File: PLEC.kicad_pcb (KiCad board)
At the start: 4 copper layers, 84 parts, among them IC1 XBP9B-DMST-002, J1 Conn_01x02, J2 Conn_01x02, J3 Conn_01x03, J4 Conn_01x06, J5 Conn_01x04, K1 PB1167, K2 PB1167, K3 PB1167, K4 PB1167, Q1 KSC2073H2TU, U1 LM1085-5.0, U2 LM1085-3.3, U3 TLP222A-2, U4 TLP222A, U5 TLP222A-2, U6 HXS20, U7 NBPMANN150, U8 Teensy3.6

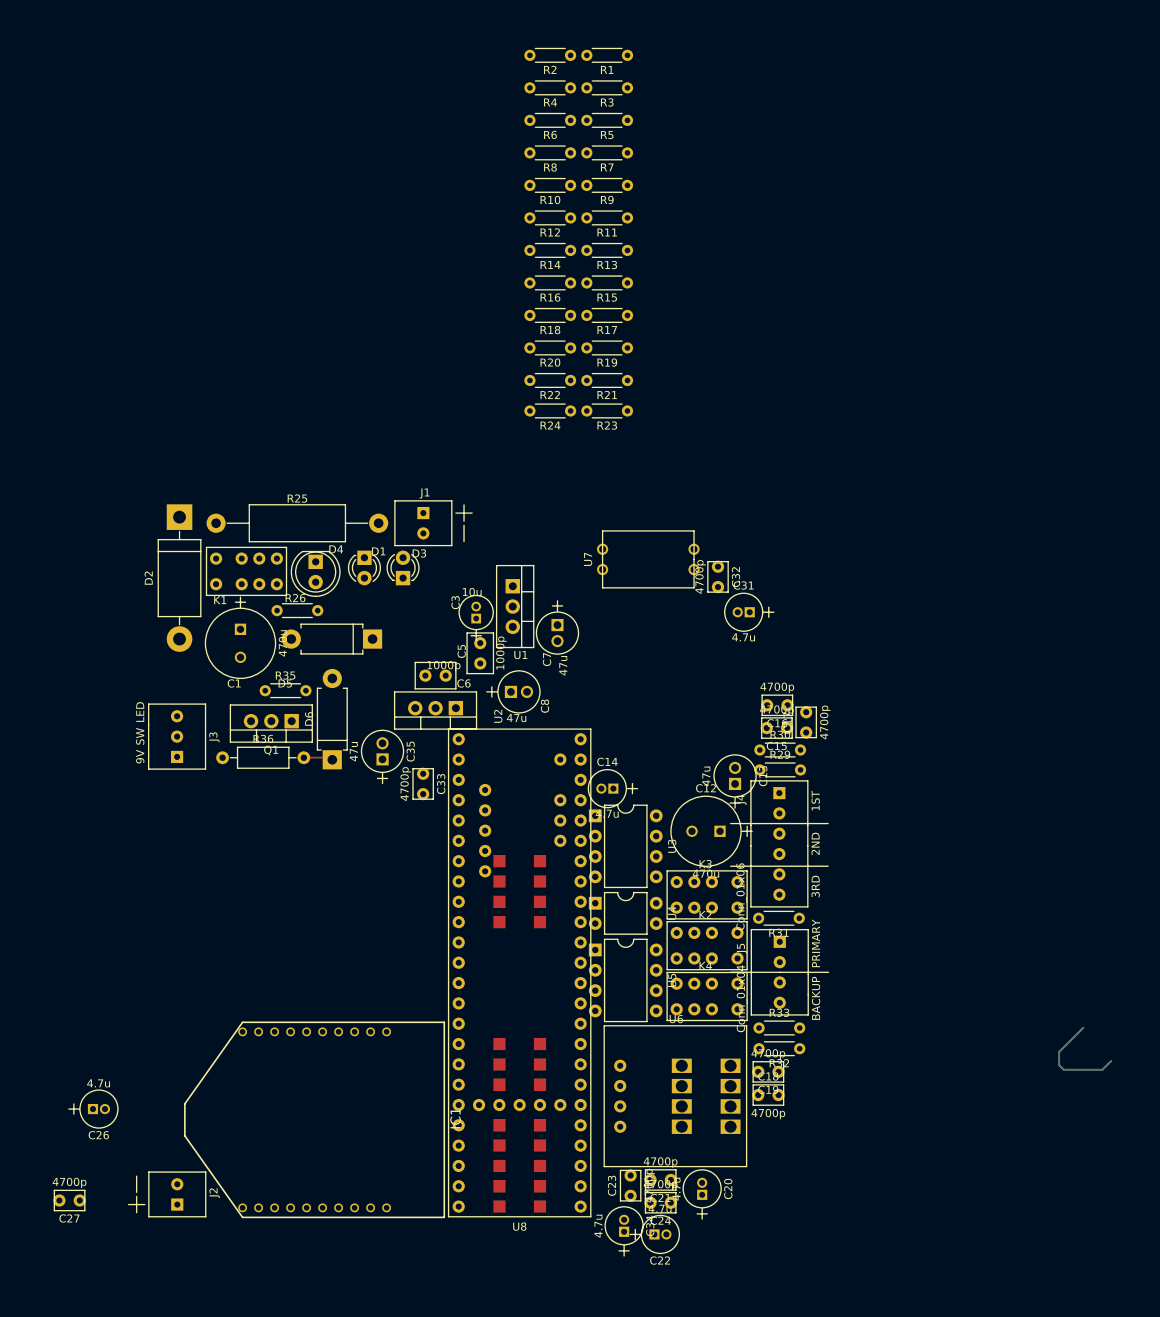
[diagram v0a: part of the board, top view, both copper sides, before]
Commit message: Almost done with layout; need to rearrange uC pins
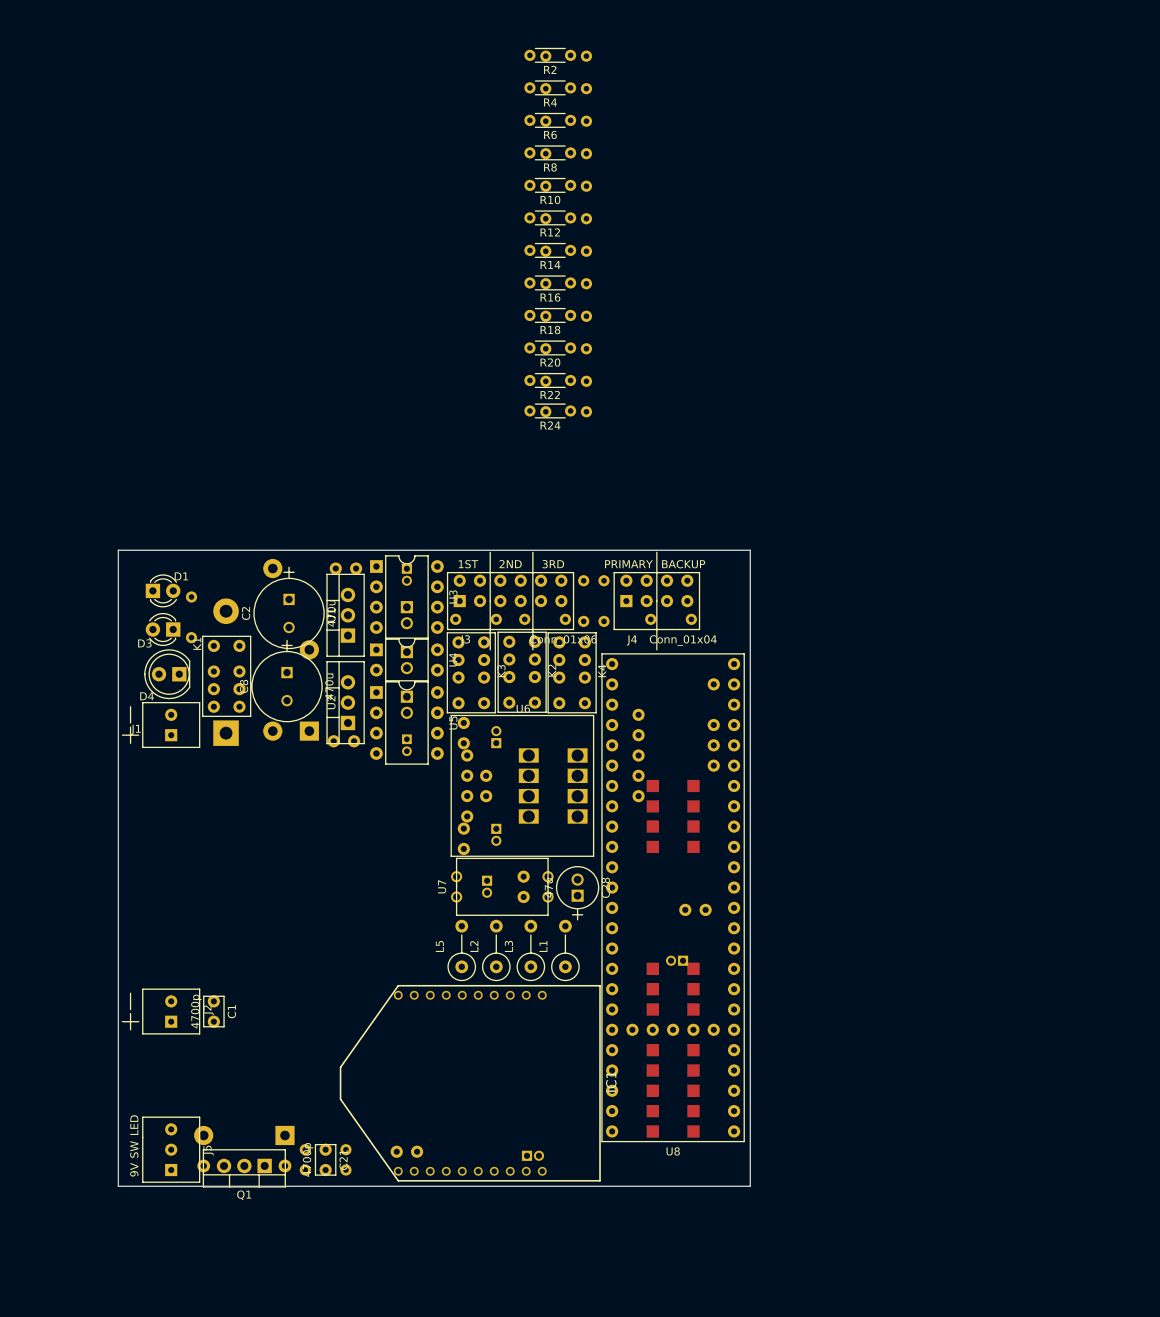
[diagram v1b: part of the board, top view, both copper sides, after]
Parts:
- removed C31, C34: 4.7u, PLEC:THTm_1.5Px4Dx7H_4.7u
- removed C32, C33: 4700p, PLEC:THTt_100Px150Lx100Wx183H_4700p
- removed C35: 47u, PLEC:THTm_2Px4Dx12H_47u
- removed R35: 100K, Resistors_THT:R_Axial_DIN0204_L3.6mm_D1.6mm_P5.08mm_Horizontal
- removed R36: 400, Resistors_THT:R_Axial_DIN0207_L6.3mm_D2.5mm_P10.16mm_Horizontal
- added C10: 4.7u, PLEC:THTm_1.5Px4Dx7H_4.7u, B.Cu at (138.9, 88.1)
- added C11: 4700p, PLEC:THTt_100Px150Lx100Wx183H_4700p, B.Cu at (146.8, 88.9)
- added C2: 470u, PLEC:THTm_5Px8Dx22H__470u, F.Cu at (124.2, 93.0)
- added C25: 4700p, PLEC:THTt_100Px150Lx100Wx183H_4700p, B.Cu at (153.5, 127.2)
- added C28: 47u, PLEC:THTm_2Px4Dx12H_47u, F.Cu at (160.3, 127.3)
- added C4: 1000p, PLEC:THTt_100Px200Lx125Wx200H_1000p, B.Cu at (131.3, 87.4)
- added C9: 47u, PLEC:THTm_2Px4Dx12H_47u, B.Cu at (138.9, 98.8)
- added L1: Ferrite_Bead_Small, Inductors_THT:L_Axial_L7.0mm_D3.3mm_P5.08mm_Vertical_Fastron_MICC, F.Cu at (158.8, 137.2)
- added L2: Ferrite_Bead_Small, Inductors_THT:L_Axial_L7.0mm_D3.3mm_P5.08mm_Vertical_Fastron_MICC, F.Cu at (150.1, 137.2)
- added L3: Ferrite_Bead_Small, Inductors_THT:L_Axial_L7.0mm_D3.3mm_P5.08mm_Vertical_Fastron_MICC, F.Cu at (154.4, 137.2)
- added L5: Ferrite_Bead_Small, Inductors_THT:L_Axial_L7.0mm_D3.3mm_P5.08mm_Vertical_Fastron_MICC, F.Cu at (145.8, 137.2)
- added R27: 100K, Resistors_THT:R_Axial_DIN0204_L3.6mm_D1.6mm_P5.08mm_Horizontal, B.Cu at (145.0, 93.7)
- added R28: 100K, Resistors_THT:R_Axial_DIN0204_L3.6mm_D1.6mm_P5.08mm_Horizontal, B.Cu at (153.7, 93.7)
- added R34: 400, Resistors_THT:R_Axial_DIN0207_L6.3mm_D2.5mm_P10.16mm_Horizontal, B.Cu at (113.5, 162.1)
- C1: value 470u -> 4700p; footprint PLEC:THTm_5Px8Dx22H__470u -> PLEC:THTt_100Px150Lx100Wx183H_4700p
- C12: value 470u -> 4700p; footprint PLEC:THTm_5Px8Dx22H__470u -> PLEC:THTt_100Px150Lx100Wx183H_4700p; moved to B.Cu
- C13: value 47u -> 4700p; footprint PLEC:THTm_2Px4Dx12H_47u -> PLEC:THTt_100Px150Lx100Wx183H_4700p; moved to B.Cu
- C14, C20, C26: value 4.7u -> 4700p; footprint PLEC:THTm_1.5Px4Dx7H_4.7u -> PLEC:THTt_100Px150Lx100Wx183H_4700p; moved to B.Cu
- C15, C17, C19, C22, C23, C3, C5, C7, D2, D5, D6, R1, R11, R13, R15, R17, R19, R21, R23, R25, R26, R29, R3, R30, R31, R32, R33, R5, R7, R9: moved to B.Cu
- C16, C18, C24, C27: value 4700p -> 4.7u; footprint PLEC:THTt_100Px150Lx100Wx183H_4700p -> PLEC:THTm_1.5Px4Dx7H_4.7u; moved to B.Cu
- C6: value 1000p -> 47u; footprint PLEC:THTt_100Px200Lx125Wx200H_1000p -> PLEC:THTm_2Px4Dx12H_47u; moved to B.Cu
- C8: value 47u -> 470u; footprint PLEC:THTm_2Px4Dx12H_47u -> PLEC:THTm_5Px8Dx22H__470u
- J3: value Conn_01x03 -> Conn_01x06; footprint PLEC:THT_TerminalBlock_2.5mm_3pos -> PLEC:THT_TerminalBlock_2.5mm_6pos
- J4: value Conn_01x06 -> Conn_01x04; footprint PLEC:THT_TerminalBlock_2.5mm_6pos -> PLEC:THT_TerminalBlock_2.5mm_4pos
- J5: value Conn_01x04 -> Conn_01x03; footprint PLEC:THT_TerminalBlock_2.5mm_4pos -> PLEC:THT_TerminalBlock_2.5mm_3pos
- moved C27 81.6 mm to (172.7, 136.4), turned to 180 degrees
- moved J5 81.2 mm to (109.5, 162.6), turned to 90 degrees
- moved C26 78.6 mm to (175.0, 130.0)
- moved R33 59.4 mm to (126.2, 162.6)
- moved R32 58.1 mm to (131.3, 160.0)
- moved C20 57.1 mm to (148.8, 114.6)
- moved C19 56.9 mm to (146.1, 108.0), turned to 90 degrees
- moved C18 56.2 mm to (150.1, 108.5), turned to 90 degrees
- moved Q1 55.7 mm to (121.2, 162.1)
- moved D6 47.3 mm to (123.7, 158.2), turned to 180 degrees
- moved C1 46.2 mm to (114.8, 142.7), turned to 90 degrees
- moved C17 45.2 mm to (146.1, 121.2)
- moved C24 45.1 mm to (149.0, 127.1), turned to 270 degrees
- moved U7 44.8 mm to (151.1, 127.2)
- moved U6 43.2 mm to (160.3, 110.7)
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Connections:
- C1 pad 1: V_9 -> Net-(C1-Pad1)
- C12 pad 1: SWITCH_RETURN -> EM_R2+
- C12 pad 2: GND -> EM_R2-
- C13 pad 1: SWITCH_RETURN -> EM_R3+
- C13 pad 2: GND -> EM_R3-
- C14 pad 1: SWITCH_RETURN -> EM_E1+
- C14 pad 2: GND -> EM_E1-
- C15 pad 1: EM_R1+ -> EM_E2+
- C15 pad 2: EM_R1- -> EM_E2-
- C16 pad 1: EM_R2+ -> CURR_REF
- C16 pad 2: EM_R2- -> GND
- C17 pad 1: EM_R3+ -> CURR_REF
- C17 pad 2: EM_R3- -> GND
- C18 pad 1: EM_E1+ -> V_5
- C18 pad 2: EM_E1- -> GND
- C19 pad 1: EM_E2+ -> V_5
- C19 pad 2: EM_E2- -> GND
- C20 pad 1: CURR_REF -> CurrentData_5V
- C21 pad 1: CURR_REF -> Net-(C21-Pad1)
- C22 pad 1: V_5 -> V_33
- C23 pad 1: V_5 -> V_33
- C24 pad 1: CurrentData_5V -> V_5
- C26 pad 1: V_33 -> V_5
- C26 pad 2: GND -> /Microcontroller/VEE
- C27 pad 1: V_33 -> V_5
- C27 pad 2: GND -> /Microcontroller/VEE
- C6 pad 1: Net-(C3-Pad1) -> V_5
- C7 pad 1: V_5 -> V_33
- C8 pad 1: V_33 -> SWITCH_RETURN
- J2 pad 1: ROVER_RELAY -> Net-(C1-Pad1)
- J2 pad 2: GND -> Net-(J2-Pad2)
- J3 pad 1: V_9 -> EM_R1+
- J3 pad 2: SWITCH_RETURN -> EM_R1-
- J3 pad 3: /LED_CATHODE -> EM_R2+
- J4 pad 1: EM_R1+ -> EM_E1+
- J4 pad 2: EM_R1- -> EM_E1-
- J4 pad 3: EM_R2+ -> EM_E2+
- J4 pad 4: EM_R2- -> EM_E2-
- J5 pad 1: EM_E1+ -> Net-(J5-Pad1)
- J5 pad 2: EM_E1- -> Net-(J5-Pad2)
- J5 pad 3: EM_E2+ -> /LED_CATHODE
- Q1 pad 1: LED_CONTROL -> Net-(C21-Pad1)
- R29 pad 1: EM_R1+ -> EM_R3+
- R29 pad 2: EM_R1- -> EM_R3-
- R30 pad 1: EM_R2+ -> EM_E1+
- R30 pad 2: EM_R2- -> EM_E1-
- R31 pad 1: EM_R3+ -> EM_E2+
- R31 pad 2: EM_R3- -> EM_E2-
- R32 pad 1: EM_E1+ -> Net-(C21-Pad1)
- R32 pad 2: EM_E1- -> LED_CONTROL
- R33 pad 1: EM_E2+ -> SWITCH_RETURN
- R33 pad 2: EM_E2- -> Net-(C21-Pad1)
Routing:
- net (no net): track 13.2 -> 0.00 mm
- net Net-(D6-Pad1): track 3.66 -> 0.00 mm
- net Net-(D2-Pad2): track 1.27 -> 0.00 mm
- net Net-(C3-Pad1): track 1.08 -> 0.00 mm
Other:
- board outline added: 79 x 79.5 mm

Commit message: Finished PCB with no errors
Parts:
- added C29: 4700p, PLEC:THTt_100Px150Lx100Wx183H_4700p, F.Cu at (114.7, 160.1)
- added G***: LOGO, PLEC:USLI_logo_820, B.Cu at (148.8, 151.6)
- added G***: LOGO, PLEC:USLI_logo_negative, F.Cu at (122.9, 149.4)
- added REF**: 1pin, Connectors:1pin, F.Cu at (110.2, 110.0)
- added REF**: 1pin, Connectors:1pin, F.Cu at (143.5, 136.4)
- added REF**: 1pin, Connectors:1pin, F.Cu at (141.5, 115.3)
- added REF**: 1pin, Connectors:1pin, F.Cu at (108.5, 151.1)
- added REF**: 1pin, Connectors:1pin, F.Cu at (173.7, 165.9)
- added REF**: 1pin, Connectors:1pin, F.Cu at (179.1, 95.8)
- added REF**: 1pin, Connectors:1pin, F.Cu at (116.1, 89.2)
- R2, R4: moved to B.Cu
- moved R2 113.2 mm to (174.1, 135.5), turned to 90 degrees
- moved R3 105.3 mm to (168.5, 132.0), turned to 90 degrees
- moved R4 101.8 mm to (170.9, 128.4), turned to 90 degrees
- moved R1 101.6 mm to (174.1, 123.3), turned to 270 degrees
- moved R9 83.0 mm to (173.0, 120.9), turned to 180 degrees
- moved R10 82.1 mm to (169.7, 120.9), turned to 0 degrees
- moved R5 79.8 mm to (178.1, 108.2), turned to 90 degrees
- moved R6 76.6 mm to (178.1, 105.7), turned to 270 degrees
- moved R11 76.6 mm to (173.0, 118.4), turned to 180 degrees
- moved R12 75.5 mm to (169.7, 118.4), turned to 0 degrees
- moved R13 70.1 mm to (173.0, 115.8), turned to 180 degrees
- moved R14 69.0 mm to (169.7, 115.8), turned to 0 degrees
- moved R7 66.1 mm to (174.4, 99.1)
- moved R8 66.0 mm to (176.9, 99.1)
- moved R15 63.7 mm to (173.0, 113.3), turned to 180 degrees
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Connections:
- net /Power Rails/VCC_9 renamed /V_Bat
- net Net-(C3-Pad1) renamed /Power Rails/V9_DIODE
- net Net-(J5-Pad1) renamed /V9_Out
- net Net-(K2-Pad4) renamed /Relays/R3D_SUPPLY
- net Net-(U6-Pad2) renamed /Current Sensor/COIL1
- net Net-(U6-Pad4) renamed /Current Sensor/COIL2
- net Net-(U6-Pad6) renamed /Current Sensor/COIL3
- C1 pad 2: GND -> Net-(C1-Pad2)
- C26 pad 2: /Microcontroller/VEE -> GND
- C27 pad 2: /Microcontroller/VEE -> GND
- C28 pad 2: /Microcontroller/VEE -> GND
- J2 pad 2: Net-(J2-Pad2) -> Net-(C1-Pad2)
- J5 pad 2: Net-(J5-Pad2) -> /SW_IN
- L3 pad 1: Net-(J5-Pad2) -> /SW_IN
- L5 pad 1: Net-(J2-Pad2) -> Net-(C1-Pad2)
- R33 pad 1: SWITCH_RETURN -> /SW_IN
- U8 pad 1: /Microcontroller/VEE -> GND
- U8 pad 10: (no net) -> ROVER_RELAY
- U8 pad 11: (no net) -> XB_~INTERRUPT
- U8 pad 13: (no net) -> SPI_MOSI
- U8 pad 14: (no net) -> SPI_MISO
- U8 pad 16: UART_~CTS -> UART_~RTS
- U8 pad 17: UART_~RTS -> UART_~CTS
- U8 pad 18: XB_~RST -> (no net)
- U8 pad 19: XB_~SLP -> SPI_CLK
- U8 pad 2: SPI_MOSI -> UART_TIXO
- U8 pad 20: XB_~INTERRUPT -> (no net)
- U8 pad 21: (no net) -> XB_~SLP
- U8 pad 22: (no net) -> XB_~RST
- U8 pad 23: SPI_SS -> EM_E2_VD-
- U8 pad 24: SPI_CLK -> EM_E2_VD+
- U8 pad 3: SPI_MISO -> UART_TOXI
- U8 pad 30: UART_TOXI -> EM_R1_VD+
- U8 pad 31: UART_TIXO -> EM_R1_VD-
- U8 pad 32: (no net) -> EM_R2_VD+
- U8 pad 33: (no net) -> EM_R2_VD-
- U8 pad 34: (no net) -> EM_R3_VD+
- U8 pad 35: (no net) -> EM_R3_VD-
- U8 pad 36: (no net) -> EM_E1_VD+
- U8 pad 37: CURR_REF -> EM_E1_VD-
- U8 pad 38: CurrentData_2.5V -> CURR_REF
- U8 pad 39: /Microcontroller/VEE -> GND
- U8 pad 41: EM_R1_VD+ -> PRESSURE+
- U8 pad 42: EM_R1_VD- -> PRESSURE-
- U8 pad 43: EM_R2_VD+ -> ARMED_3V
- U8 pad 44: EM_R2_VD- -> CurrentData_2.5V
- U8 pad 45: EM_R3_VD+ -> RELAY_1_DRAIN
- U8 pad 46: EM_R3_VD- -> RELAY_2_DRAIN
- U8 pad 47: EM_E1_VD+ -> RELAY_3_DRAIN
- U8 pad 48: EM_E1_VD- -> SPI_SS
- U8 pad 49: EM_E2_VD+ -> RELAY_4_DRAIN
- U8 pad 50: EM_E2_VD- -> RELAY_5_DRAIN
- U8 pad 7: (no net) -> RLY_12_SHNT_SRC
- U8 pad 8: (no net) -> RLY_3_SHNT_SRC
- U8 pad 9: (no net) -> RLY_45_SHNT_SRC
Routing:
- net SWITCH_RETURN: track 0.00 -> 145.1 mm, vias 0 -> 1
- net V_9: track 0.00 -> 111.7 mm
- net EM_E1+: track 0.00 -> 107.5 mm, vias 0 -> 1
- net SPI_CLK: track 0.00 -> 103.9 mm
- net /SW_IN: track 0.00 -> 93.0 mm
- net EM_R3+: track 0.00 -> 89.2 mm, vias 0 -> 2
- net XB_~RST: track 0.00 -> 86.9 mm, vias 0 -> 2
- net RELAY_1_DRAIN: track 0.00 -> 81.9 mm, vias 0 -> 2
- net EM_R1+: track 0.00 -> 81.0 mm, vias 0 -> 3
- net XB_~SLP: track 0.00 -> 78.5 mm, vias 0 -> 2
- net RELAY_2_DRAIN: track 0.00 -> 77.8 mm, vias 0 -> 2
- net RELAY_3_DRAIN: track 0.00 -> 74.7 mm, vias 0 -> 2
- net RELAY_4_DRAIN: track 0.00 -> 73.4 mm, vias 0 -> 1
- net SPI_MISO: track 0.00 -> 73.2 mm
- net EM_R2+: track 0.00 -> 73.0 mm, vias 0 -> 5
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- added copper zone on In2.Cu, net /V_Bat
- added copper zone on In2.Cu, net SWITCH_RETURN
- added copper zone on In2.Cu, net V_33
- added copper zone on In2.Cu, net V_9
- removed copper zone on B.Cu, net V_9
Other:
- board size 79 x 79.5 mm -> 80.3 x 83.8 mm
- net class 3A added: clearance 0.2, trace_width 0.508, via_dia 1.524, via_drill 0.762
- board text added: "7-24V"
- board text added: "Designed by b.t.anderson@me.com Schematics at https://github.com/bradAnders/kicad_PLEC"
- board text added: "PROPERTY OF"
